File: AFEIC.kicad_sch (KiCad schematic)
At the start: 19 parts, among them J1 CONN HEADER VERT 6POS 1.5MM, U1 TLE9012DQUXUMA1

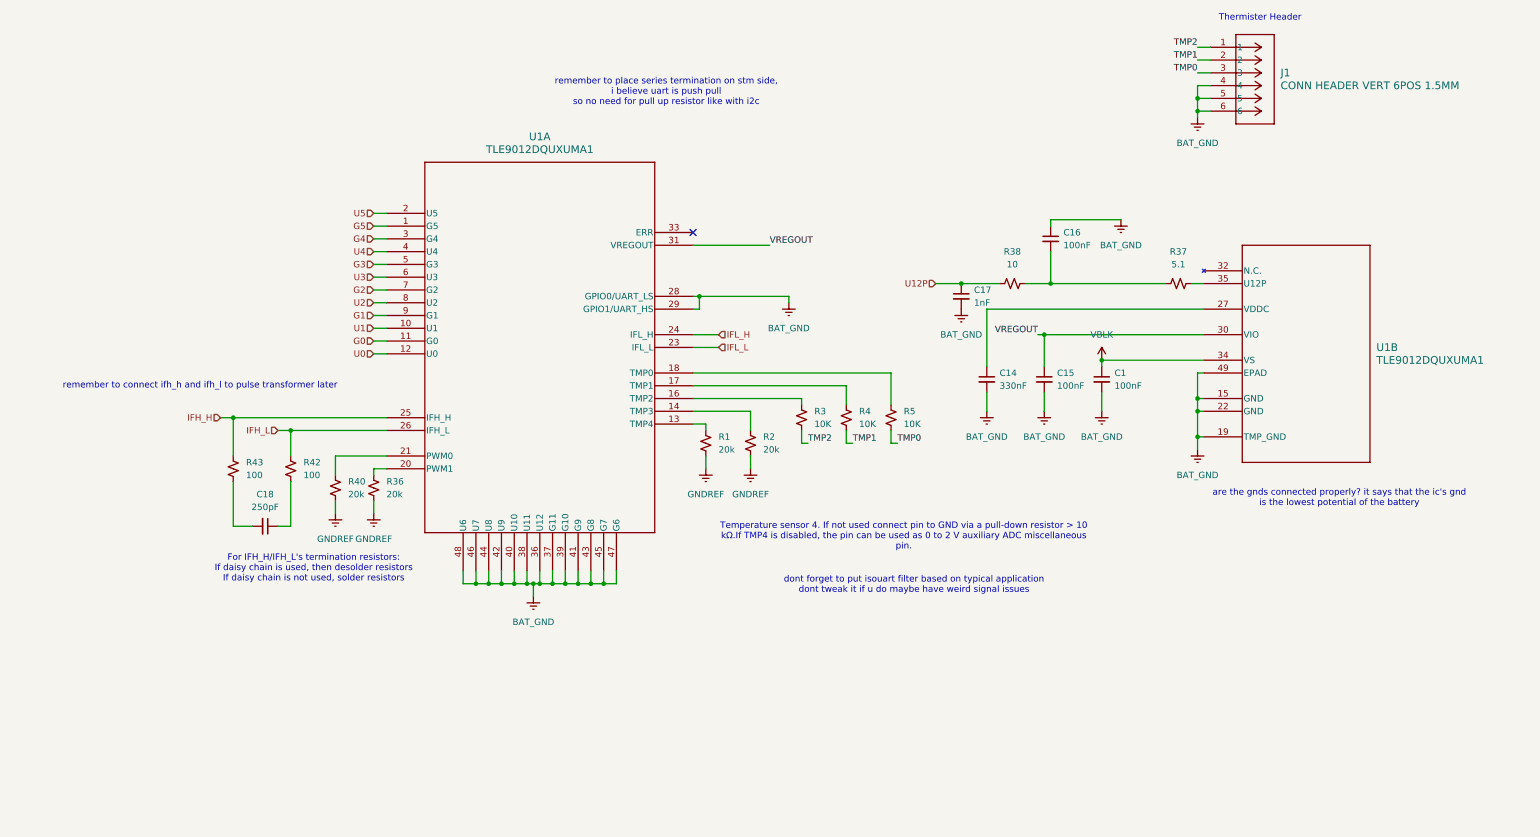
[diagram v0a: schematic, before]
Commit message: schematic done except for pulse transformer
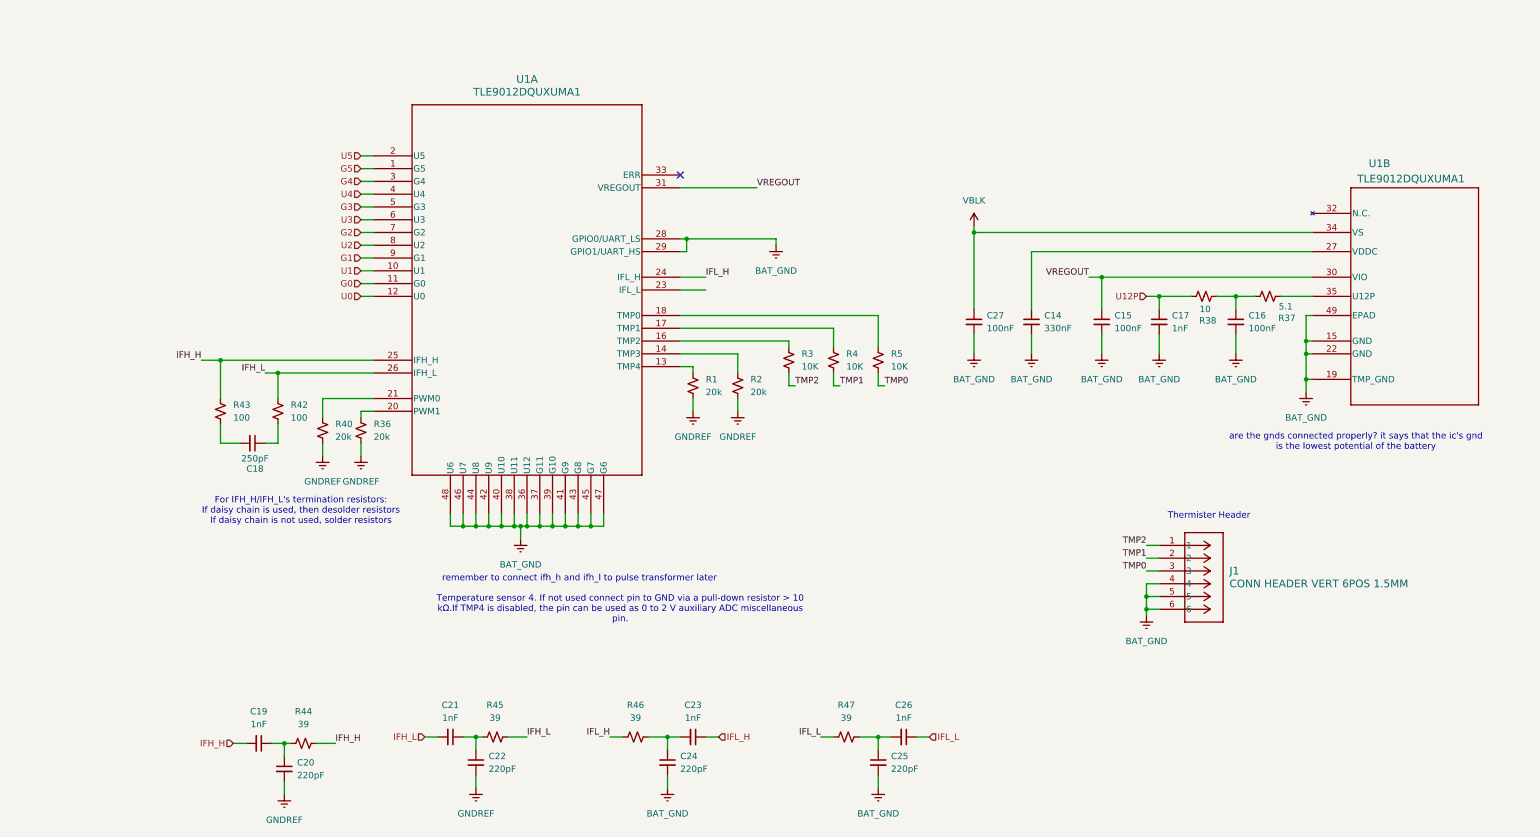
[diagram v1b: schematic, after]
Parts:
- removed C1: 100nF, symbol Device:C_Small
- added C19, C21, C23, C26: 1nF, symbol Device:C_Small
- added C20, C22, C24, C25: 220pF, symbol Device:C_Small
- added C27: 100nF, symbol Device:C_Small
- added R44, R45, R46, R47: 39, symbol Device:R_Small_US
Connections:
- net BAT_GND: now also C16.2, C24.2, C25.2, C27.2; no longer C16.1
- net GNDREF: now also C20.2, C22.2
- net IFH_H: now also C19.2, R44.2
- net IFH_L: now also C21.2, R45.2
- net IFL_H: now also C23.1, R46.1
- net IFL_L: now also C26.1, R47.1; no longer U1.23 (IFL_L)
- net VBLK: now also C27.1
- net at R37.1, R38.2: now also C16.1; no longer C16.2
- new net: C19.1, C20.1, R44.1
- new net: C23.2, C24.1, R46.2
- new net: C25.1, C26.2, R47.2
- new net: C21.1, C22.1, R45.1
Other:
- note removed: "dont forget to put isouart filter based on typical application dont tweak it if u do maybe have weird signal issues"
- note removed: "remember to place series termination on stm side, i believe uart is push pull so no need for pull up resistor like with i2c"
- moved on the sheet: C14, C15, C18, J1, R1, R2, R3, R36, R4, R40, R42, R43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

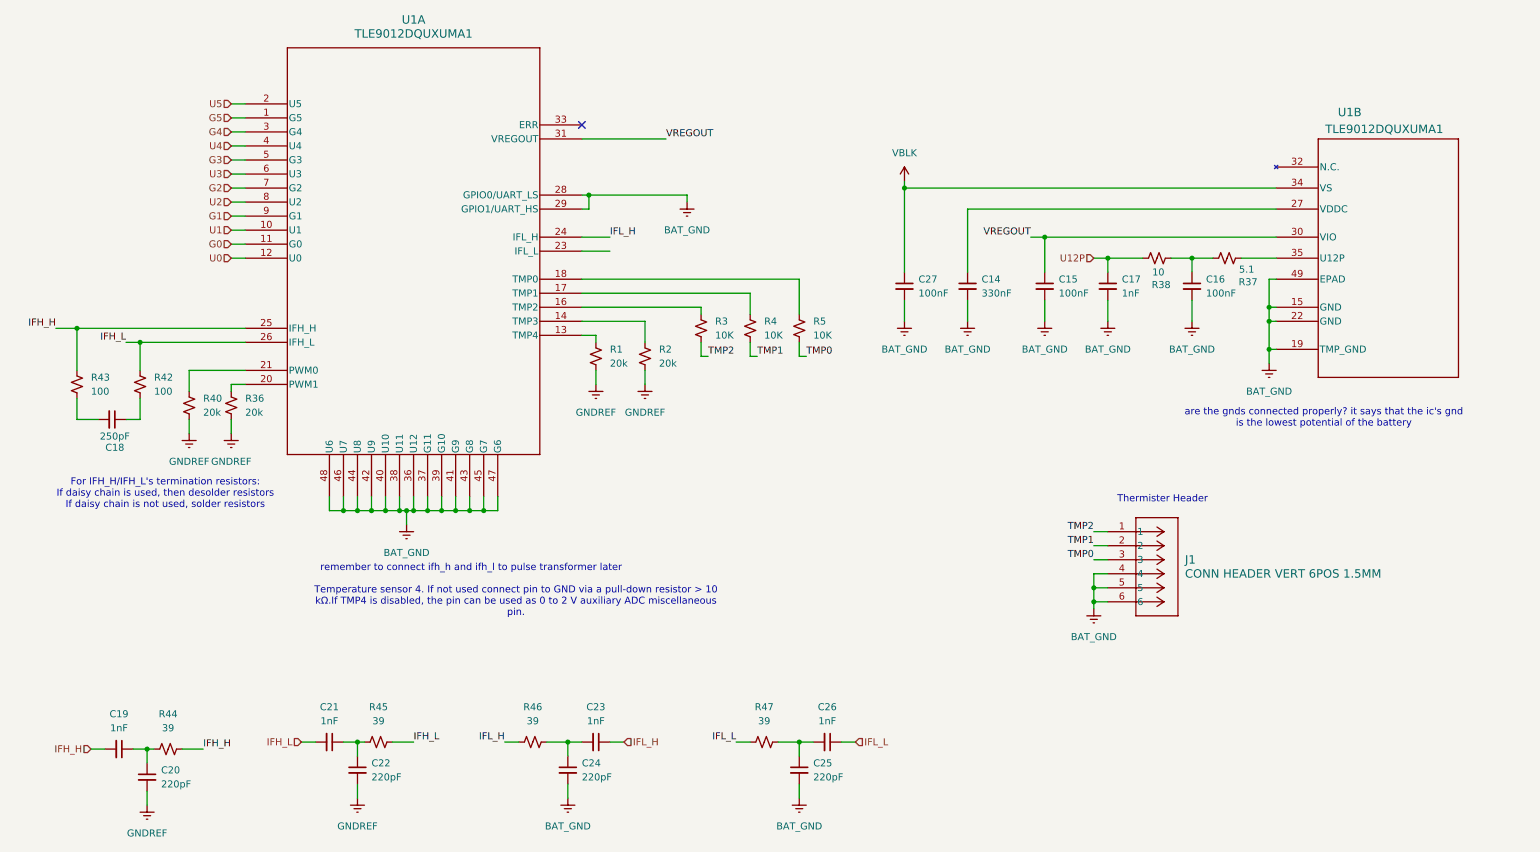
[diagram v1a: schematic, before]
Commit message: fixed balancing module and added pulse transformer
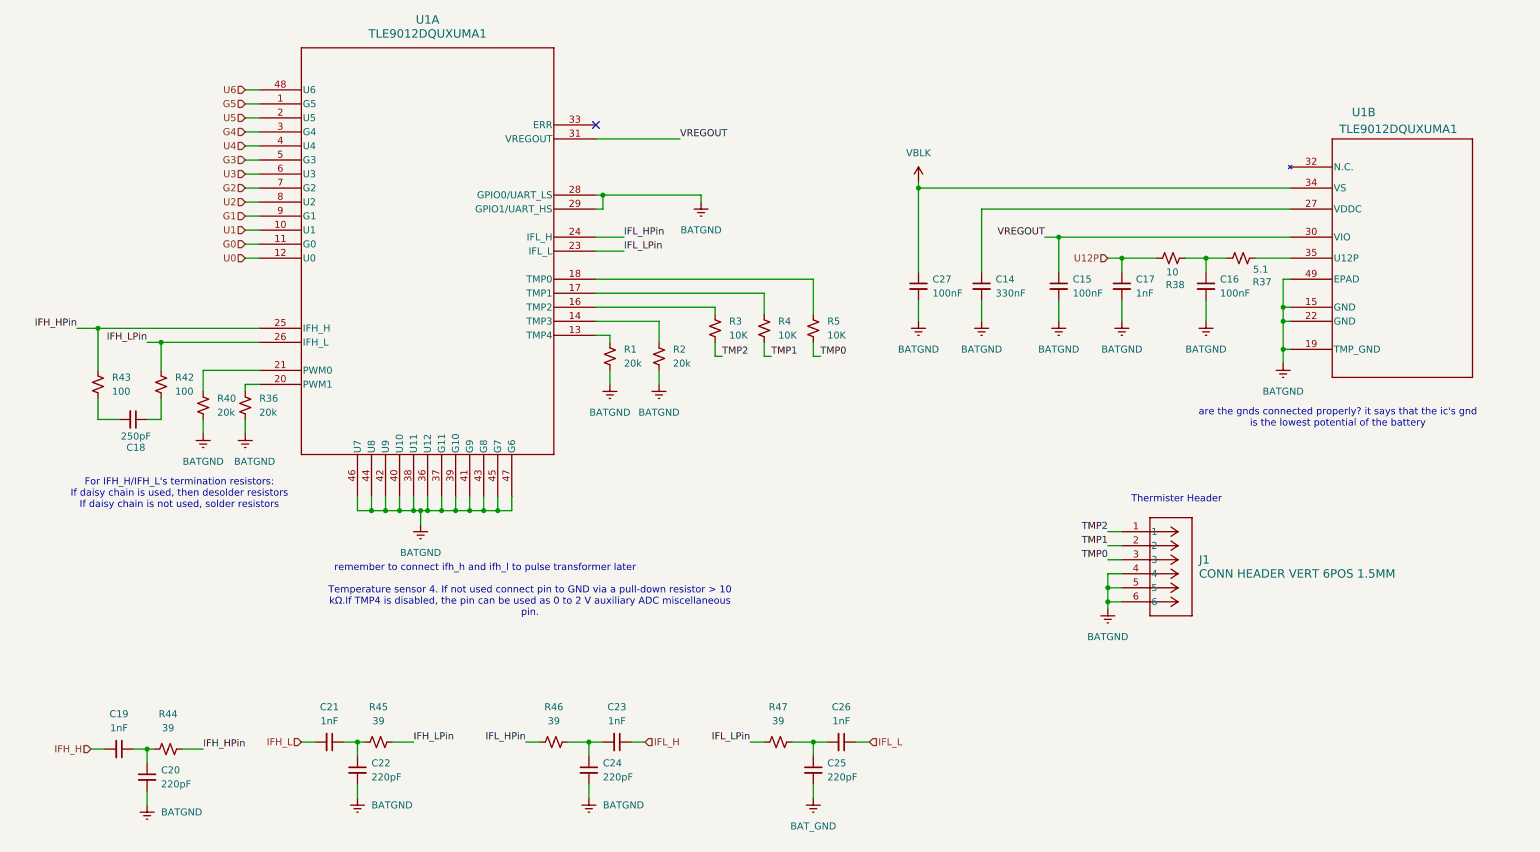
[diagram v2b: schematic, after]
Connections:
- net BAT_GND: no longer C14.2, C15.2, C16.2, C17.2, C24.2, C27.2, J1.4, J1.5, J1.6, U1.15 (GND), U1.19 (TMP_GND), U1.22 (GND), U1.28 (GPIO0/UART_LS), U1.29 (GPIO1/UART_HS), U1.36 (U12), U1.37 (G11), U1.38 (U11), U1.39 (G10), U1.40 (U10), U1.41 (G9), U1.42 (U9), U1.43 (G8), U1.44 (U8), U1.45 (G7), U1.46 (U7), U1.47 (G6), U1.48 (U6), U1.49 (EPAD)
- net IFH_H: no longer R43.1, R44.2, U1.25 (IFH_H)
- net IFH_L: no longer R42.1, R45.2, U1.26 (IFH_L)
- net IFL_H: no longer R46.1, U1.24 (IFL_H)
- net IFL_L: no longer R47.1
- net IFL_LPin: now reaches U1.23 (IFL_L)
- net IFL_LPin: now also R47.1
- net GNDREF renamed BATGND
- net BATGND: now also C14.2, C15.2, C16.2, C17.2, C24.2, C27.2, J1.4, J1.5, J1.6, U1.15 (GND), U1.19 (TMP_GND), U1.22 (GND), U1.28 (GPIO0/UART_LS), U1.29 (GPIO1/UART_HS), U1.36 (U12), U1.37 (G11), U1.38 (U11), U1.39 (G10), U1.40 (U10), U1.41 (G9), U1.42 (U9), U1.43 (G8), U1.44 (U8), U1.45 (G7), U1.46 (U7), U1.47 (G6), U1.49 (EPAD)
- new net IFH_HPin: R43.1, R44.2, U1.25 (IFH_H)
- new net IFH_LPin: R42.1, R45.2, U1.26 (IFH_L)
- new net IFL_HPin: R46.1, U1.24 (IFL_H)
- new net U6: U1.48 (U6)
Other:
- moved on the sheet: C14, C15, C16, C17, C18, C23, C24, C25, C26, C27, J1, R1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

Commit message: finished schematic
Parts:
- removed R3, R4, R5: 10K, symbol Device:R_Small_US
- added C18, C21, C25: 10nF, symbol Device:C_Small
- added C20, C22, C26: 4.7nF, symbol Device:C_Small
- added R22: 100, symbol Device:R_Small_US
- added R23, R25: 10K, symbol Device:R_Small_US
- renumbered C18 to C14, C19 to C15, C20 to C16, C21 to C17, C22 to C19, C24 to C23, C23 to C24, C25 to C27, C26 to C28, C27 to C29, C14 to C30, C15 to C31, C17 to C32, C16 to C33, J1 to J4, R43 to R14, R42 to R15, R40 to R16, R36 to R17, R44 to R18, R1 to R19, R2 to R20, R45 to R21, R46 to R24, R47 to R26, R38 to R27, R37 to R28
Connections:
- net BATGND: now also C18.2, C20.2, C21.2, C22.2, C25.2, C26.2
- net TMP0: now also C26.1, R25.2
- net TMP1: now also C22.1, R23.2
- net TMP2: now also C20.1, R22.2
- net at U1.17 (TMP1): now also C21.1, R23.1
- net at U1.16 (TMP2): now also C18.1, R22.1
- net at U1.18 (TMP0): now also C25.1, R25.1
- net IFH_HPin renamed IFH_H_Filt
- net IFH_LPin renamed IFH_L_Filt
- net IFL_HPin renamed IFL_H_Filt
- net IFL_LPin renamed IFL_L_Filt
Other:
- note removed: "Temperature sensor 4. If not used connect pin to GND via a pull-down resistor > 10 kΩ.If TMP4 is disabled, the pin can be used as 0 to 2 V auxiliary ADC miscellaneous pin."
- note removed: "are the gnds connected properly? it says that the ic's gnd is the lowest potential of the battery"
- note removed: "remember to connect ifh_h and ifh_l to pulse transformer later"
- moved on the sheet: C14, C15, C16, C17, C19, C23, C24, C27, C28, C29, C30, C31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

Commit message: passive values
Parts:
- removed C22, C26: 4.7nF, symbol Device:C_Small
- removed C31, C33: 100nF, symbol Device:C_Small
- added C44, C45, C46, C47: CAP CER 0.1UF 25V X7R 0603, Capacitor_SMD:C_0603_1608Metric, symbol Device:C_Small
- added C52, C53: CAP CER 0.33UF 16V X7R 0603, Capacitor_SMD:C_0603_1608Metric, symbol Device:C_Small
- C14: value 250pF -> CAP CER 250PF 25V NP0 0603; footprint (none) -> Capacitor_SMD:C_0603_1608Metric
- C15, C17, C24, C28, C32: value 1nF -> CAP CER 0603 1NF 16V X7R 10%; footprint (none) -> Capacitor_SMD:C_0603_1608Metric
- C16, C19, C23, C27: value 220pF -> CAP CER 220PF 50V X7R 0603; footprint (none) -> Capacitor_SMD:C_0603_1608Metric
- C18, C21: value 10nF -> CAP CER 0603 4.7NF 16V X7R 10%; footprint (none) -> Capacitor_SMD:C_0603_1608Metric
- C20: value 4.7nF -> CAP CER 0603 4.7NF 16V X7R 10%; footprint (none) -> Capacitor_SMD:C_0603_1608Metric
- C25: value 10nF -> CAP CER 10NF 16V X7R 0603; footprint (none) -> Capacitor_SMD:C_0603_1608Metric
- C29: value 100nF -> CAP CER 10NF 16V X7R 0603; footprint (none) -> Capacitor_SMD:C_0603_1608Metric
- C30: value 330nF -> CAP CER 10NF 16V X7R 0603; footprint (none) -> Capacitor_SMD:C_0603_1608Metric
- R14, R15, R22: value 100 -> RES 100 OHM 1% 1/10W 0603; footprint (none) -> Resistor_SMD:R_0603_1608Metric
- R16, R17, R19, R20: value 20k -> RES 20K OHM 1% 1/10W 0603; footprint (none) -> Capacitor_SMD:C_0603_1608Metric
- R18, R21, R24, R26: value 39 -> RES SMD 39 OHM 5% 1/8W 0603; footprint (none) -> Resistor_SMD:R_0603_1608Metric; LCSC (none) -> C2079967
- R23, R25: value 10K -> RES SMD 10K OHM 1% 1/8W 0603; footprint (none) -> Resistor_SMD:R_0603_1608Metric; LCSC (none) -> C844918
- R27: value 10 -> RES 10 OHM 1% 1/10W 0603; footprint (none) -> Resistor_SMD:R_0603_1608Metric
- R28: value 5.1 -> RES SMD 5.1 OHM 1% 1/8W 0603; footprint (none) -> Resistor_SMD:R_0603_1608Metric; LCSC (none) -> C242492
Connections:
- net BATGND: now also C32.1, C44.2, C45.2, C46.2, C47.2; no longer C32.2
- net IFH_H: now also C15.1; no longer C15.2
- net IFH_H_Filt: now also R14.2; no longer R14.1
- net IFH_L: now also C17.1; no longer C17.2
- net IFH_L_Filt: now also R15.2; no longer R15.1
- net IFL_H: now also C24.2; no longer C24.1
- net IFL_L: now also C28.2; no longer C28.1
- net TMP0: now also C21.1
- net TMP1: now also C20.1
- net TMP2: now also C18.1; no longer C20.1
- net U12P: now also C32.2; no longer C32.1
- net VBLK: now also C44.1; no longer C29.1
- net VREGOUT: now also C47.1
- net at R23.1, U1.17 (TMP1): now also C30.1; no longer C21.1
- net at C16.1, R18.1: now also C15.2; no longer C15.1
- net at C23.1, R24.2: now also C24.1; no longer C24.2
- net at C27.1, R26.2: now also C28.1; no longer C28.2
- net at C19.1, R21.1: now also C17.2; no longer C17.1
- net at U1.27 (VDDC): now also C45.1; no longer C30.1
- net at R27.2, R28.1: now also C46.1
- net at C14.2: now also R14.1; no longer R14.2
- net at C14.1: now also R15.1; no longer R15.2
- net at R22.1, U1.16 (TMP2): now also C29.1; no longer C18.1
